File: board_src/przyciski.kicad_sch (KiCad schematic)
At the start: 9 parts, among them J5 Conn_01x08

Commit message: wersja 3d
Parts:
- removed SW10, SW3, SW4, SW5, SW6, SW7, SW8, SW9: ~, Button_Switch_THT:SW_PUSH_6mm, symbol Switch:SW_Push
- added S10, S3, S4, S5, S6, S7, S8, S9: 1301.9319, footprints:przycisk, symbol przycisk:1301.9319
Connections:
- net GND: now also S10.3 (COM_1), S3.3 (COM_1), S4.3 (COM_1), S5.3 (COM_1), S6.3 (COM_1), S7.3 (COM_1), S8.3 (COM_1), S9.3 (COM_1)
- net at J5.1 (Pin_1): now also S3.1 (NO_1)
- net at J5.2 (Pin_2): now also S4.1 (NO_1)
- net at J5.3 (Pin_3): now also S5.1 (NO_1)
- net at J5.4 (Pin_4): now also S6.1 (NO_1)
- net at J5.5 (Pin_5): now also S7.1 (NO_1)
- net at J5.6 (Pin_6): now also S8.1 (NO_1)
- net at J5.7 (Pin_7): now also S9.1 (NO_1)
- net at J5.8 (Pin_8): now also S10.1 (NO_1)
- no-connect marks 0 -> 16
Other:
- moved on the sheet: J5

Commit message: wersja z FT232RN
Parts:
- added SW1: SW_MEC_5E, Button_Switch_THT:SW_PUSH_6mm_H9.5mm, symbol Switch:SW_MEC_5E
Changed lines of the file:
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@@
+	)
+	(symbol
+		(lib_id "Switch:SW_MEC_5E")
+		(at 83.82 113.03 0)
+		(unit 1)
+		(exclude_from_sim no)
+		(in_bom yes)
+		(on_board yes)
+		(dnp no)
+		(fields_autoplaced yes)
+		(property "Reference" "SW1"
+			(at 83.82 102.87 0)
+			(effects
+				(font
+					(size 1.27 1.27)
+				)
+			)
+		)
+		(property "Value" "SW_MEC_5E"
+			(at 83.82 105.41 0)
+			(effects
+				(font
+					(size 1.27 1.27)
+				)
+			)
+		)
+		(property "Footprint" "Button_Switch_THT:SW_PUSH_6mm_H9.5mm"
+			(at 83.82 105.41 0)
+			(effects
+				(font
+					(size 1.27 1.27)
+				)
+				(hide yes)
+			)
+		)
+		(property "Datasheet" "http://www.apem.com/int/index.php?controller=attachment&id_attachment=1371"
+			(at 83.82 105.41 0)
+			(effects
+				(font
+					(size 1.27 1.27)
+				)
+				(hide yes)
+			)
+		)
+		(property "Description" "MEC 5E single pole normally-open tactile switch"
+			(at 83.82 113.03 0)
+			(effects
+				(font
+					(size 1.27 1.27)
+				)
+				(hide yes)
+			)
+		)
+		(pin "4"
+		)
+		(pin "2"
+		)
+		(pin "1"
+		)
+		(pin "3"
+		)
+		(instances
+			(project ""
+				(path "/772e9f49-cfcf-4cf6-843d-0684684f2d4b/55a14567-f1b3-493a-ad76-30ad6f394af6"
+					(reference "SW1")
+					(unit 1)
+				)
+			)
+		)
 	)
 	(symbol

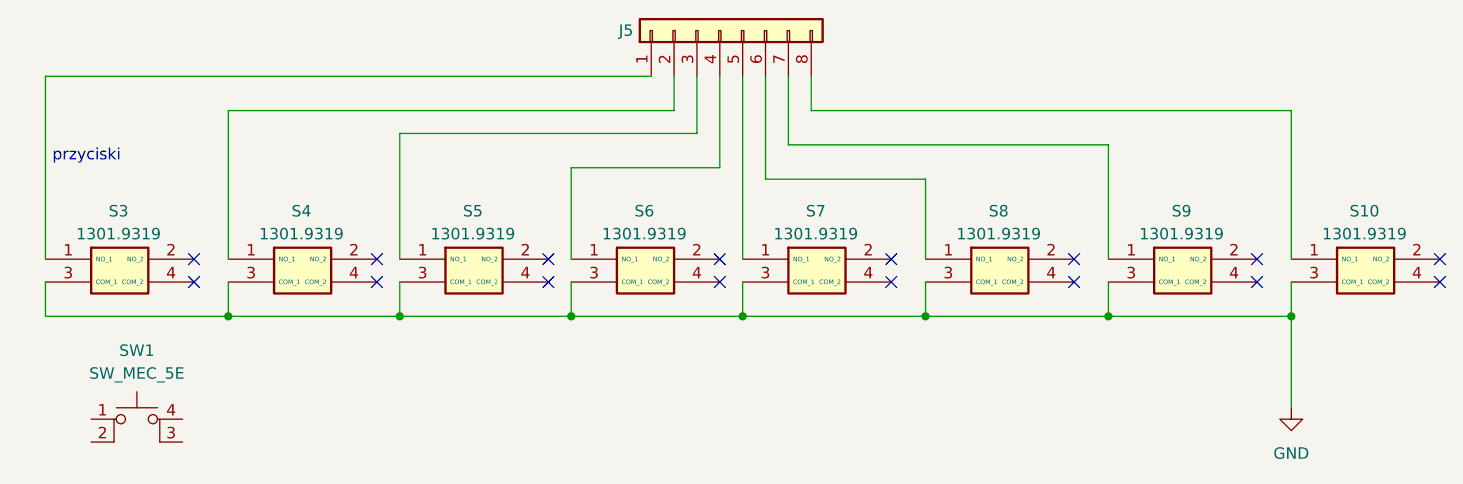
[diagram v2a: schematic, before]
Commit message: Wersja ze sciezkami miedzianymi
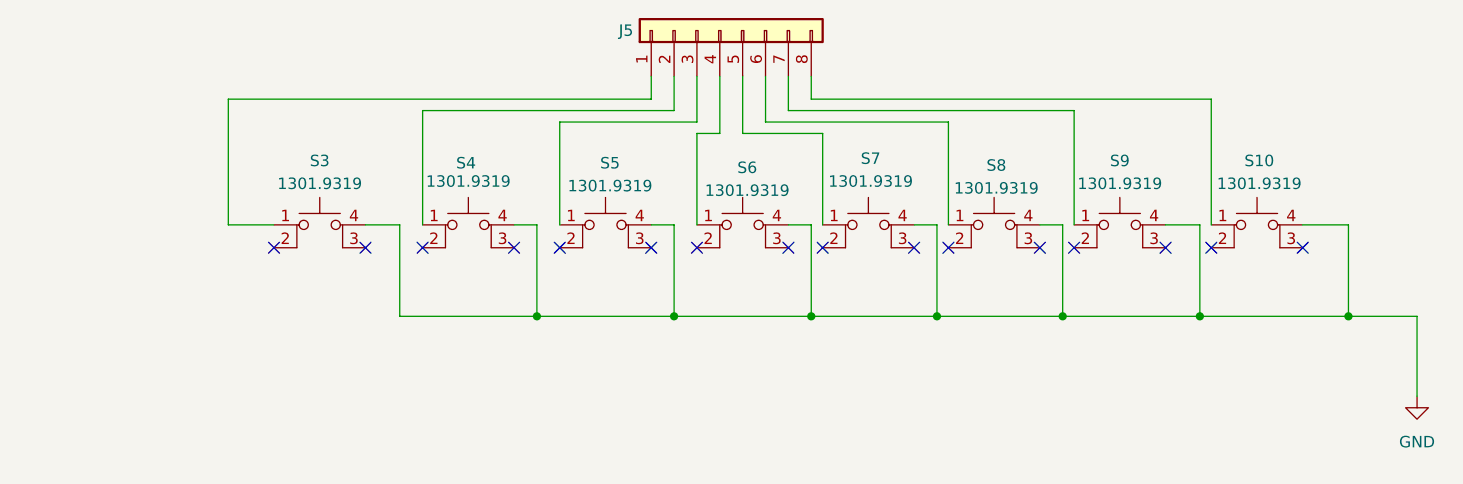
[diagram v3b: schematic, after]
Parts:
- removed SW1: SW_MEC_5E, Button_Switch_THT:SW_PUSH_6mm_H9.5mm, symbol Switch:SW_MEC_5E
- S10, S3, S4, S5, S6, S7, S8, S9: footprint footprints:przycisk -> Button_Switch_THT:SW_PUSH_6mm_H9.5mm; symbol przycisk:1301.9319 -> Switch:SW_MEC_5E
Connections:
- net GND: now also S10.4 (A), S3.4 (A), S4.4 (A), S5.4 (A), S6.4 (A), S7.4 (A), S8.4 (A), S9.4 (A); no longer S10.3 (COM_1), S3.3 (COM_1), S4.3 (COM_1), S5.3 (COM_1), S6.3 (COM_1), S7.3 (COM_1), S8.3 (COM_1), S9.3 (COM_1)
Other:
- note removed: "przyciski"
- moved on the sheet: S10, S3, S4, S5, S6, S7, S8, S9

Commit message: poprawione polaczenia diod i wartosci opornikow, aktualizacja niektorych elementow ze wzgledu na braki w magazynie
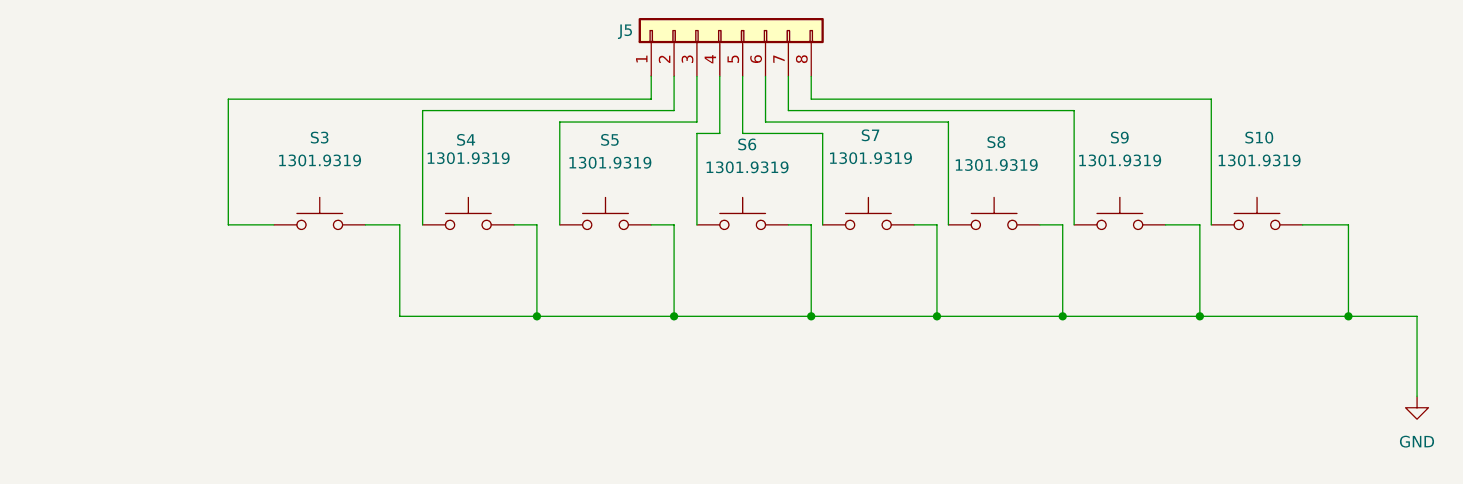
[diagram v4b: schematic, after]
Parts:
- S10, S3, S4, S5, S6, S7, S8, S9: symbol Switch:SW_MEC_5E -> Switch:SW_Push
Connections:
- net GND: now also S10.2, S3.2, S4.2, S5.2, S6.2, S7.2, S8.2, S9.2; no longer S10.4 (A), S3.4 (A), S4.4 (A), S5.4 (A), S6.4 (A), S7.4 (A), S8.4 (A), S9.4 (A)
- no-connect marks 16 -> 0

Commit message: Poprawki w schematach. Rozpoczęte korekty płytki
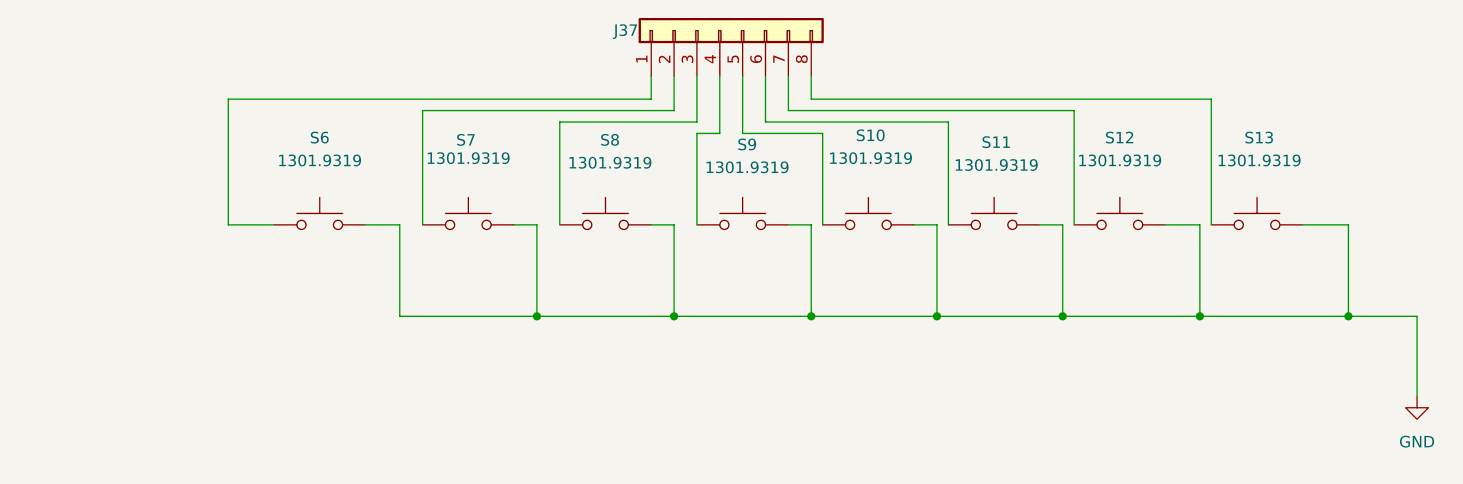
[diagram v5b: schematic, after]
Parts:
- J37: renamed from J5; footprint Connector_PinHeader_2.54mm:PinHeader_1x08_P2.54mm_Vertical -> Connector_PinSocket_2.54mm:PinSocket_1x20_P2.54mm_Vertical
- S11: renamed from S8; footprint Button_Switch_THT:SW_PUSH_6mm_H9.5mm -> footprints:JS102011CQN
- S13: renamed from S10; footprint Button_Switch_THT:SW_PUSH_6mm_H9.5mm -> footprints:JS102011CQN
- renumbered S7 to S10, S9 to S12, S3 to S6, S4 to S7, S5 to S8, S6 to S9
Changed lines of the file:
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@@
 		(on_board yes)
 		(dnp no)
-		(property "Reference" "J5"
+		(property "Reference" "J37"
 			(at 138.176 67.31 90)
 			(effects
@@
 			)
 		)
-		(property "Footprint" "Connector_PinHeader_2.54mm:PinHeader_1x08_P2.54mm_Vertical"
+		(property "Footprint" "Connector_PinSocket_2.54mm:PinSocket_1x20_P2.54mm_Vertical"
 			(at 148.59 67.31 0)
 			(effects
@@
 			(project "board"
 				(path "/772e9f49-cfcf-4cf6-843d-0684684f2d4b/55a14567-f1b3-493a-ad76-30ad6f394af6"
-					(reference "J5")
+					(reference "J37")
 					(unit 1)
 				)
@@
 		(on_board yes)
 		(dnp no)
-		(property "Reference" "S8"
+		(property "Reference" "S11"
 			(at 179.324 79.756 0)
 			(effects
@@
 			)
 		)
-		(property "Footprint" "Button_Switch_THT:SW_PUSH_6mm_H9.5mm"
+		(property "Footprint" "footprints:JS102011CQN"
 			(at 179.07 81.28 0)
 			(effects
@@
 			(project "board"
 				(path "/772e9f49-cfcf-4cf6-843d-0684684f2d4b/55a14567-f1b3-493a-ad76-30ad6f394af6"
-					(reference "S8")
+					(reference "S11")
 					(unit 1)
 				)
@@
 		(on_board yes)
 		(dnp no)
-		(property "Reference" "S7"
+		(property "Reference" "S10"
 			(at 165.354 78.994 0)
 			(effects
@@
 			(project "board"
 				(path "/772e9f49-cfcf-4cf6-843d-0684684f2d4b/55a14567-f1b3-493a-ad76-30ad6f394af6"
-					(reference "S7")
+					(reference "S10")
 					(unit 1)
 				)
@@
 		(on_board yes)
 		(dnp no)
-		(property "Reference" "S10"
+		(property "Reference" "S13"
 			(at 208.534 79.248 0)
 			(effects
@@
 			)
 		)
-		(property "Footprint" "Button_Switch_THT:SW_PUSH_6mm_H9.5mm"
+		(property "Footprint" "footprints:JS102011CQN"
 			(at 208.28 81.28 0)
 			(effects
@@
 			(project "board"
 				(path "/772e9f49-cfcf-4cf6-843d-0684684f2d4b/55a14567-f1b3-493a-ad76-30ad6f394af6"
-					(reference "S10")
+					(reference "S13")
 					(unit 1)
 				)
@@
 		(on_board yes)
 		(dnp no)
-		(property "Reference" "S5"
+		(property "Reference" "S8"
 			(at 136.398 79.502 0)
 			(effects
@@
 			(project "board"
 				(path "/772e9f49-cfcf-4cf6-843d-0684684f2d4b/55a14567-f1b3-493a-ad76-30ad6f394af6"
-					(reference "S5")
+					(reference "S8")
 					(unit 1)
 				)
@@
 		(on_board yes)
 		(dnp no)
-		(property "Reference" "S3"
+		(property "Reference" "S6"
 			(at 104.14 79.248 0)
 			(effects
@@
 			(project "board"
 				(path "/772e9f49-cfcf-4cf6-843d-0684684f2d4b/55a14567-f1b3-493a-ad76-30ad6f394af6"
-					(reference "S3")
+					(reference "S6")
 					(unit 1)
 				)
@@
 		(on_board yes)
 		(dnp no)
-		(property "Reference" "S9"
+		(property "Reference" "S12"
 			(at 193.04 79.248 0)
 			(effects
@@
 			(project "board"
 				(path "/772e9f49-cfcf-4cf6-843d-0684684f2d4b/55a14567-f1b3-493a-ad76-30ad6f394af6"
-					(reference "S9")
+					(reference "S12")
 					(unit 1)
 				)
@@
 		(on_board yes)
 		(dnp no)
-		(property "Reference" "S4"
+		(property "Reference" "S7"
 			(at 120.396 79.502 0)
 			(effects
@@
 			(project "board"
 				(path "/772e9f49-cfcf-4cf6-843d-0684684f2d4b/55a14567-f1b3-493a-ad76-30ad6f394af6"
-					(reference "S4")
+					(reference "S7")
 					(unit 1)
 				)
@@
 		(dnp no)
 		(fields_autoplaced yes)
-		(property "Reference" "#PWR020"
+		(property "Reference" "#PWR071"
 			(at 226.06 114.3 0)
 			(effects
@@
 			(project "board"
 				(path "/772e9f49-cfcf-4cf6-843d-0684684f2d4b/55a14567-f1b3-493a-ad76-30ad6f394af6"
-					(reference "#PWR020")
+					(reference "#PWR071")
 					(unit 1)
 				)
@@
 		(on_board yes)
 		(dnp no)
-		(property "Reference" "S6"
+		(property "Reference" "S9"
 			(at 151.638 80.01 0)
 			(effects
@@
 			(project "board"
 				(path "/772e9f49-cfcf-4cf6-843d-0684684f2d4b/55a14567-f1b3-493a-ad76-30ad6f394af6"
-					(reference "S6")
+					(reference "S9")
 					(unit 1)
 				)

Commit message: Wprowadzono usprawnienia i poprawki. Wersja ostateczna, wysłana do JLCPCB.
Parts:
- J37: footprint Connector_PinSocket_2.54mm:PinSocket_1x20_P2.54mm_Vertical -> Connector_PinHeader_2.54mm:PinHeader_1x08_P2.54mm_Vertical
- S11, S13: footprint footprints:JS102011CQN -> Button_Switch_THT:SW_PUSH_6mm_H9.5mm
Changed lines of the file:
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@@
 			)
 		)
-		(property "Footprint" "Connector_PinSocket_2.54mm:PinSocket_1x20_P2.54mm_Vertical"
+		(property "Footprint" "Connector_PinHeader_2.54mm:PinHeader_1x08_P2.54mm_Vertical"
 			(at 148.59 67.31 0)
 			(effects
@@
 			)
 		)
-		(property "Footprint" "footprints:JS102011CQN"
+		(property "Footprint" "Button_Switch_THT:SW_PUSH_6mm_H9.5mm"
 			(at 179.07 81.28 0)
 			(effects
@@
 			)
 		)
-		(property "Footprint" "footprints:JS102011CQN"
+		(property "Footprint" "Button_Switch_THT:SW_PUSH_6mm_H9.5mm"
 			(at 208.28 81.28 0)
 			(effects
